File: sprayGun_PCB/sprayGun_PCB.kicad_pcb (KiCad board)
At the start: 4 copper layers, 123.4 x 98.1 mm, 45 parts, among them IC1 L78S05CV, J1 PWR IN, J10 Analog IO, J11 Digital IO, J12 CAN1 termination, J13 CAN1, J14 CAN1 pin header, J15 ESC terminal, J16 VESC terminal, J17 SERVO terminal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

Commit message: This revision was sent to JLC for production.
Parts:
- J1: value PWR IN -> locked
- U2: value SN65HVD266D -> SN65HVD253D; footprint libraries:SN65HVD266D -> libraries:SN65HVD253D
- moved U2 0.31 mm to (108.5, 120.0)
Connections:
- J17 pad 2: +5VA -> +5V
- J8 pad 2: +5VA -> +5V
- U2 pad 5: unconnected-(U2-Pad5) -> GND
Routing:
- net +5V: track 133.0 -> 189.6 mm, vias 0 -> 1
- net +5VA: track 231.4 -> 213.3 mm, vias 1 -> 2
- net /RXD: track 23.8 -> 20.4 mm
- net GND: track 6.38 -> 9.45 mm
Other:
- board text added: "+ PWR IN -"
- board text added: "Every machine is a smoke machine if you operate it wrong enough."
- board text removed: "Made by Humans on Earth"

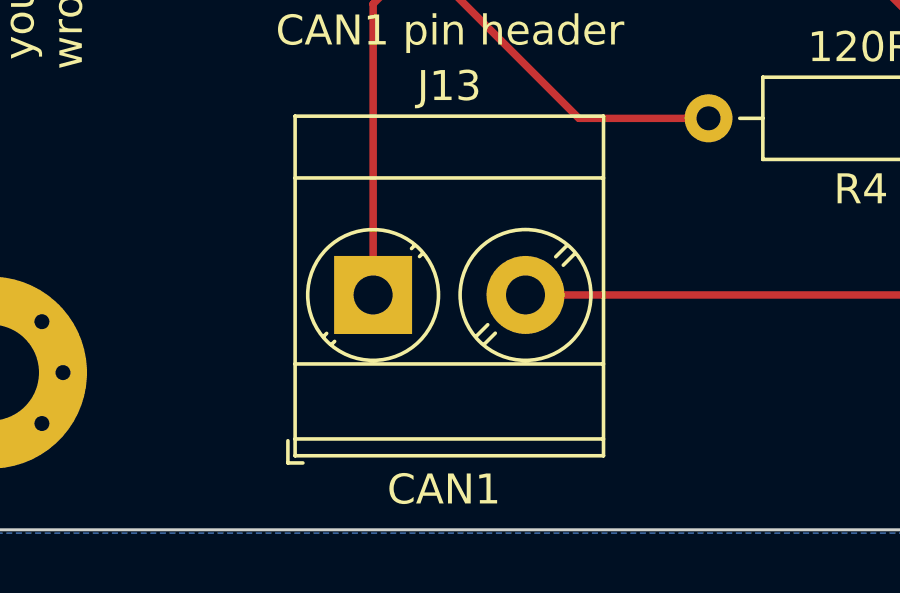
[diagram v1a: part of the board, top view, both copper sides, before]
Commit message: Exported step file o of PCB.
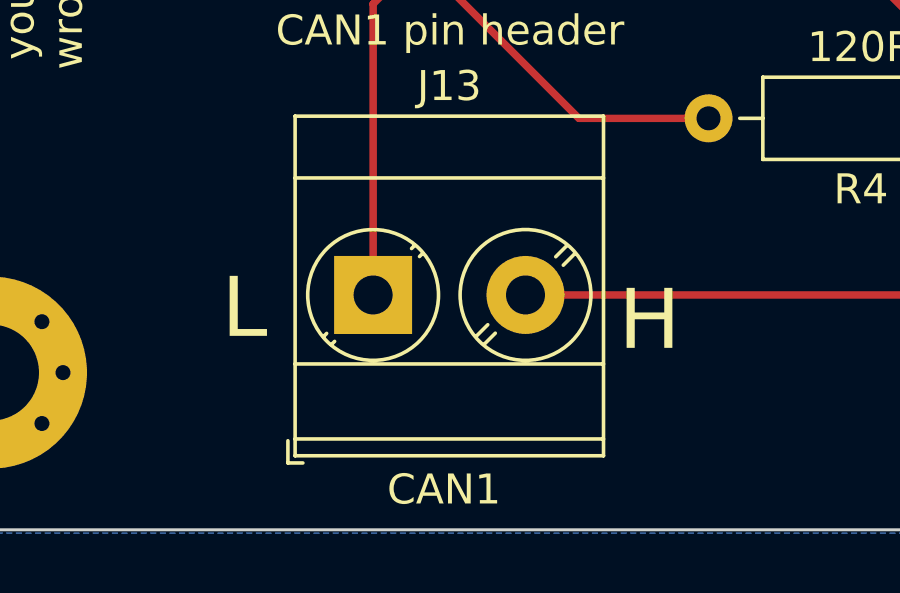
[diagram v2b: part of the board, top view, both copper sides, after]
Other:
- board text added: "H"
- board text added: "L"
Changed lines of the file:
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@@
   )
   (paper "A4")
+  (title_block
+    (title "B.Sc spray gun PCB")
+    (date "2022-04-21")
+    (rev "A")
+    (company "B.Sc Group 10")
+  )
   (layers
     (0 "F.Cu" signal)
@@
       (sketchpadsonfab false)
       (subtractmaskfromsilk true)
-      (outputformat 1)
+      (outputformat 5)
       (mirror false)
       (drillshape 0)
@@
       (rotate (xyz 0 0 0))
     )
+    (model "${KICAD6_3DMODEL_DIR}/Connector_PinSocket_2.54mm.3dshapes/PinSocket_1x15_P2.54mm_Vertical.step"
+      (offset (xyz 0 0 0))
+      (scale (xyz 1 1 1))
+      (rotate (xyz 0 0 0))
+    )
+    (model "${KICAD6_3DMODEL_DIR}/Connector_PinSocket_2.54mm.3dshapes/PinSocket_1x15_P2.54mm_Vertical.step"
+      (offset (xyz 15 0 0))
+      (scale (xyz 1 1 1))
+      (rotate (xyz 0 0 0))
+    )
   )
   (footprint "libraries:SN65HVD253D" (layer "F.Cu")
@@
     (effects (font (size 1.5 1.5) (thickness 0.3)))
   )
+  (gr_text "L" (at 101.5 137.5) (layer "F.SilkS")
+    (effects (font (size 2 2) (thickness 0.15)))
+  )
   (gr_text "+ PWR IN -" (at 159.2 48.1) (layer "F.SilkS")
     (effects (font (size 1 1) (thickness 0.15)))
@@
     (effects (font (size 1 1) (thickness 0.25)))
   )
+  (gr_text "H" (at 115 137.9) (layer "F.SilkS")
+    (effects (font (size 2 2) (thickness 0.15)) (justify mirror))
+  )
   (dimension (type aligned) (layer "In1.Cu")
-    (pts (xy 211.202 46.83) (xy 211.202 144.89))
+    (pts (xy 215.9 46.24) (xy 215.9 144.3))
     (height 0)
-    (gr_text "98.0600 mm" (at 209.402 95.86 90) (layer "In1.Cu")
+    (gr_text "98.0600 mm" (at 214.1 95.27 90) (layer "In1.Cu")
       (effects (font (size 1.5 1.5) (thickness 0.3)))
     )
